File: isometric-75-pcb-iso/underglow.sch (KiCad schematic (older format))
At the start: 36 parts, among them U301 74LVC1G125

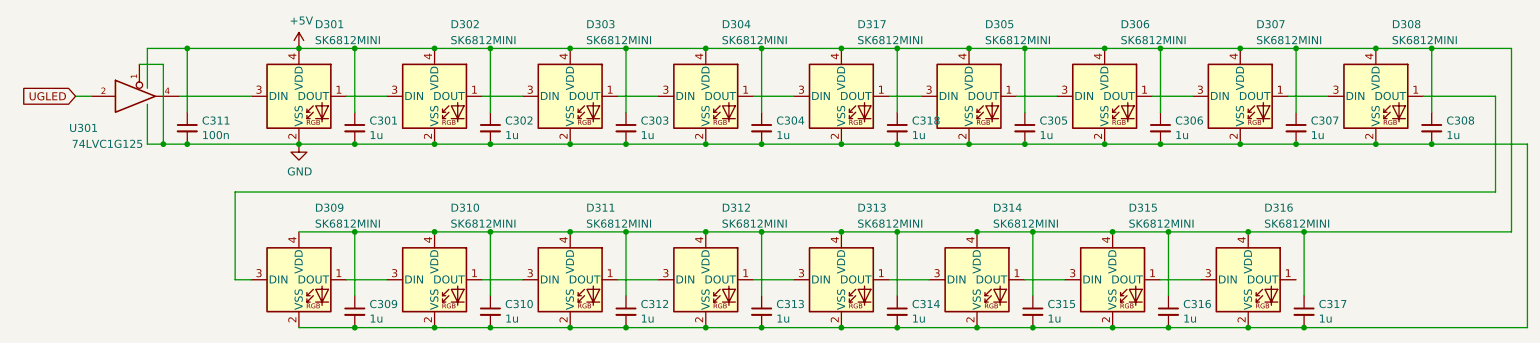
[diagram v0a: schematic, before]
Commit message: added ground planes, various minor fixes
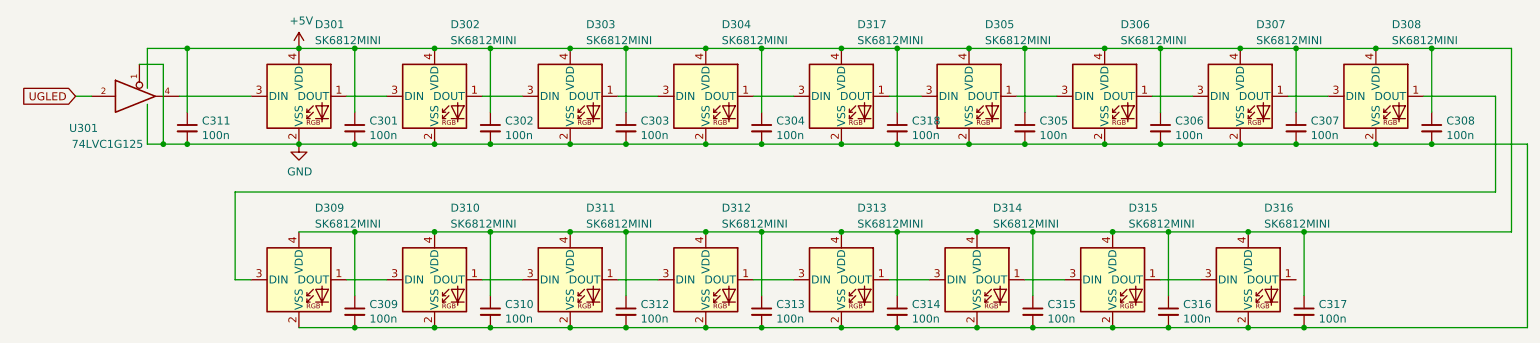
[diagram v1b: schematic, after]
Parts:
- C301, C302, C303, C304, C305, C306, C307, C308, C309, C310, C312, C313, C314, C315, C316, C317, C318: value 1u -> 100n; footprint Capacitor_SMD:C_0603_1608Metric -> Capacitor_SMD:C_0402_1005Metric
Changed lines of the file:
@@
 AR Path="/5E6E13F7/5E6E4592" Ref="C301"  Part="1"
 F 0 "C301" H 3092 1696 50  0000 L CNN
-F 1 "1u" H 3092 1605 50  0000 L CNN
-F 2 "Capacitor_SMD:C_0603_1608Metric" H 3000 1650 50  0001 C CNN
+F 1 "100n" H 3092 1605 50  0000 L CNN
+F 2 "Capacitor_SMD:C_0402_1005Metric" H 3000 1650 50  0001 C CNN
 F 3 "~" H 3000 1650 50  0001 C CNN
 	1    3000 1650
@@
 AR Path="/5E6E13F7/5E6FDF24" Ref="C302"  Part="1"
 F 0 "C302" H 3942 1696 50  0000 L CNN
-F 1 "1u" H 3942 1605 50  0000 L CNN
-F 2 "Capacitor_SMD:C_0603_1608Metric" H 3850 1650 50  0001 C CNN
+F 1 "100n" H 3942 1605 50  0000 L CNN
+F 2 "Capacitor_SMD:C_0402_1005Metric" H 3850 1650 50  0001 C CNN
 F 3 "~" H 3850 1650 50  0001 C CNN
 	1    3850 1650
@@
 AR Path="/5E6E13F7/5E704C33" Ref="C303"  Part="1"
 F 0 "C303" H 4792 1696 50  0000 L CNN
-F 1 "1u" H 4792 1605 50  0000 L CNN
-F 2 "Capacitor_SMD:C_0603_1608Metric" H 4700 1650 50  0001 C CNN
+F 1 "100n" H 4792 1605 50  0000 L CNN
+F 2 "Capacitor_SMD:C_0402_1005Metric" H 4700 1650 50  0001 C CNN
 F 3 "~" H 4700 1650 50  0001 C CNN
 	1    4700 1650
@@
 AR Path="/5E6E13F7/5E704C42" Ref="C304"  Part="1"
 F 0 "C304" H 5642 1696 50  0000 L CNN
-F 1 "1u" H 5642 1605 50  0000 L CNN
-F 2 "Capacitor_SMD:C_0603_1608Metric" H 5550 1650 50  0001 C CNN
+F 1 "100n" H 5642 1605 50  0000 L CNN
+F 2 "Capacitor_SMD:C_0402_1005Metric" H 5550 1650 50  0001 C CNN
 F 3 "~" H 5550 1650 50  0001 C CNN
 	1    5550 1650
@@
 AR Path="/5E6E13F7/5E710C99" Ref="C305"  Part="1"
 F 0 "C305" H 7292 1696 50  0000 L CNN
-F 1 "1u" H 7292 1605 50  0000 L CNN
-F 2 "Capacitor_SMD:C_0603_1608Metric" H 7200 1650 50  0001 C CNN
+F 1 "100n" H 7292 1605 50  0000 L CNN
+F 2 "Capacitor_SMD:C_0402_1005Metric" H 7200 1650 50  0001 C CNN
 F 3 "~" H 7200 1650 50  0001 C CNN
 	1    7200 1650
@@
 AR Path="/5E6E13F7/5E710CA8" Ref="C306"  Part="1"
 F 0 "C306" H 8142 1696 50  0000 L CNN
-F 1 "1u" H 8142 1605 50  0000 L CNN
-F 2 "Capacitor_SMD:C_0603_1608Metric" H 8050 1650 50  0001 C CNN
+F 1 "100n" H 8142 1605 50  0000 L CNN
+F 2 "Capacitor_SMD:C_0402_1005Metric" H 8050 1650 50  0001 C CNN
 F 3 "~" H 8050 1650 50  0001 C CNN
 	1    8050 1650
@@
 AR Path="/5E6E13F7/5E710CB7" Ref="C307"  Part="1"
 F 0 "C307" H 8992 1696 50  0000 L CNN
-F 1 "1u" H 8992 1605 50  0000 L CNN
-F 2 "Capacitor_SMD:C_0603_1608Metric" H 8900 1650 50  0001 C CNN
+F 1 "100n" H 8992 1605 50  0000 L CNN
+F 2 "Capacitor_SMD:C_0402_1005Metric" H 8900 1650 50  0001 C CNN
 F 3 "~" H 8900 1650 50  0001 C CNN
 	1    8900 1650
@@
 AR Path="/5E6E13F7/5E710CC6" Ref="C308"  Part="1"
 F 0 "C308" H 9842 1696 50  0000 L CNN
-F 1 "1u" H 9842 1605 50  0000 L CNN
-F 2 "Capacitor_SMD:C_0603_1608Metric" H 9750 1650 50  0001 C CNN
+F 1 "100n" H 9842 1605 50  0000 L CNN
+F 2 "Capacitor_SMD:C_0402_1005Metric" H 9750 1650 50  0001 C CNN
 F 3 "~" H 9750 1650 50  0001 C CNN
 	1    9750 1650
@@
 AR Path="/5E6E13F7/5E714331" Ref="C309"  Part="1"
 F 0 "C309" H 3092 2846 50  0000 L CNN
-F 1 "1u" H 3092 2755 50  0000 L CNN
-F 2 "Capacitor_SMD:C_0603_1608Metric" H 3000 2800 50  0001 C CNN
+F 1 "100n" H 3092 2755 50  0000 L CNN
+F 2 "Capacitor_SMD:C_0402_1005Metric" H 3000 2800 50  0001 C CNN
 F 3 "~" H 3000 2800 50  0001 C CNN
 	1    3000 2800
@@
 AR Path="/5E6E13F7/5E714340" Ref="C310"  Part="1"
 F 0 "C310" H 3942 2846 50  0000 L CNN
-F 1 "1u" H 3942 2755 50  0000 L CNN
-F 2 "Capacitor_SMD:C_0603_1608Metric" H 3850 2800 50  0001 C CNN
+F 1 "100n" H 3942 2755 50  0000 L CNN
+F 2 "Capacitor_SMD:C_0402_1005Metric" H 3850 2800 50  0001 C CNN
 F 3 "~" H 3850 2800 50  0001 C CNN
 	1    3850 2800
@@
 AR Path="/5E6E13F7/5E7ECFEE" Ref="C312"  Part="1"
 F 0 "C312" H 4792 2846 50  0000 L CNN
-F 1 "1u" H 4792 2755 50  0000 L CNN
-F 2 "Capacitor_SMD:C_0603_1608Metric" H 4700 2800 50  0001 C CNN
+F 1 "100n" H 4792 2755 50  0000 L CNN
+F 2 "Capacitor_SMD:C_0402_1005Metric" H 4700 2800 50  0001 C CNN
 F 3 "~" H 4700 2800 50  0001 C CNN
 	1    4700 2800
@@
 AR Path="/5E6E13F7/5E7ECFFD" Ref="C313"  Part="1"
 F 0 "C313" H 5642 2846 50  0000 L CNN
-F 1 "1u" H 5642 2755 50  0000 L CNN
-F 2 "Capacitor_SMD:C_0603_1608Metric" H 5550 2800 50  0001 C CNN
+F 1 "100n" H 5642 2755 50  0000 L CNN
+F 2 "Capacitor_SMD:C_0402_1005Metric" H 5550 2800 50  0001 C CNN
 F 3 "~" H 5550 2800 50  0001 C CNN
 	1    5550 2800
@@
 AR Path="/5E6E13F7/5E7FCA18" Ref="C314"  Part="1"
 F 0 "C314" H 6492 2846 50  0000 L CNN
-F 1 "1u" H 6492 2755 50  0000 L CNN
-F 2 "Capacitor_SMD:C_0603_1608Metric" H 6400 2800 50  0001 C CNN
+F 1 "100n" H 6492 2755 50  0000 L CNN
+F 2 "Capacitor_SMD:C_0402_1005Metric" H 6400 2800 50  0001 C CNN
 F 3 "~" H 6400 2800 50  0001 C CNN
 	1    6400 2800
@@
 AR Path="/5E6E13F7/5E7FCA27" Ref="C315"  Part="1"
 F 0 "C315" H 7342 2846 50  0000 L CNN
-F 1 "1u" H 7342 2755 50  0000 L CNN
-F 2 "Capacitor_SMD:C_0603_1608Metric" H 7250 2800 50  0001 C CNN
+F 1 "100n" H 7342 2755 50  0000 L CNN
+F 2 "Capacitor_SMD:C_0402_1005Metric" H 7250 2800 50  0001 C CNN
 F 3 "~" H 7250 2800 50  0001 C CNN
 	1    7250 2800
@@
 AR Path="/5E6E13F7/5E7FCA37" Ref="C316"  Part="1"
 F 0 "C316" H 8192 2846 50  0000 L CNN
-F 1 "1u" H 8192 2755 50  0000 L CNN
-F 2 "Capacitor_SMD:C_0603_1608Metric" H 8100 2800 50  0001 C CNN
+F 1 "100n" H 8192 2755 50  0000 L CNN
+F 2 "Capacitor_SMD:C_0402_1005Metric" H 8100 2800 50  0001 C CNN
 F 3 "~" H 8100 2800 50  0001 C CNN
 	1    8100 2800
@@
 AR Path="/5E6E13F7/5E7FCA46" Ref="C317"  Part="1"
 F 0 "C317" H 9042 2846 50  0000 L CNN
-F 1 "1u" H 9042 2755 50  0000 L CNN
-F 2 "Capacitor_SMD:C_0603_1608Metric" H 8950 2800 50  0001 C CNN
+F 1 "100n" H 9042 2755 50  0000 L CNN
+F 2 "Capacitor_SMD:C_0402_1005Metric" H 8950 2800 50  0001 C CNN
 F 3 "~" H 8950 2800 50  0001 C CNN
 	1    8950 2800
@@
 AR Path="/5E6E13F7/5E8DE968" Ref="C318"  Part="1"
 F 0 "C318" H 6492 1696 50  0000 L CNN
-F 1 "1u" H 6492 1605 50  0000 L CNN
-F 2 "Capacitor_SMD:C_0603_1608Metric" H 6400 1650 50  0001 C CNN
+F 1 "100n" H 6492 1605 50  0000 L CNN
+F 2 "Capacitor_SMD:C_0402_1005Metric" H 6400 1650 50  0001 C CNN
 F 3 "~" H 6400 1650 50  0001 C CNN
 	1    6400 1650

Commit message: cosmethical changes, fixed a footprint collision
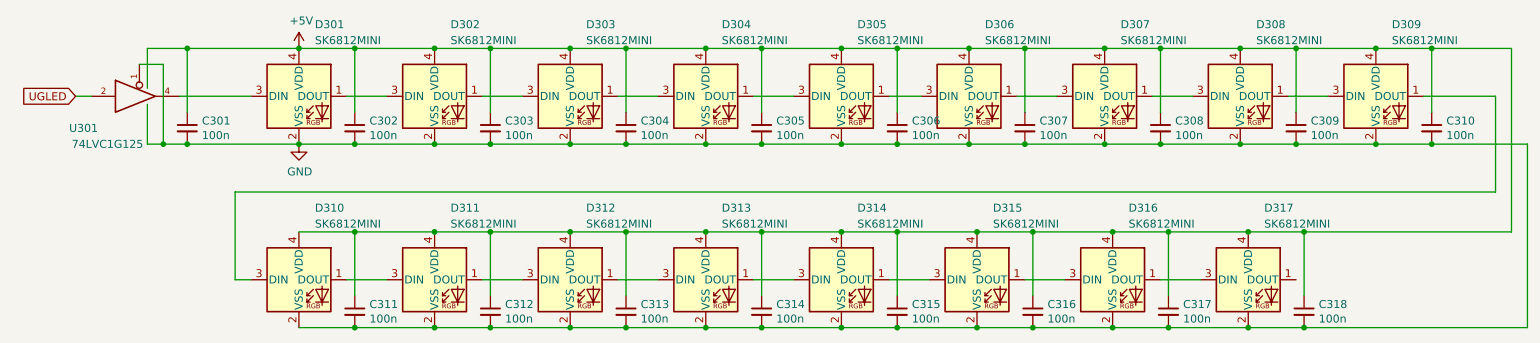
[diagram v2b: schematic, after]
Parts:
- renumbered C311 to C301, C301 to C302, C302 to C303, C303 to C304, C304 to C305, C318 to C306, C305 to C307, C306 to C308, C307 to C309, C308 to C310, C309 to C311, C310 to C312, C312 to C313, C313 to C314, C314 to C315, C315 to C316, C316 to C317, C317 to C318, D317 to D305, D305 to D306, D306 to D307, D307 to D308, D308 to D309, D309 to D310, D310 to D311, D311 to D312, D312 to D313, D313 to D314, D314 to D315, D315 to D316, D316 to D317
